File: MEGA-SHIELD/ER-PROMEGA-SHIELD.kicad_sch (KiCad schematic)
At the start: 1 part

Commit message: feat: cambios
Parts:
- added J10, J4, J6, J7, J9: Screw_Terminal_01x10, symbol Connector:Screw_Terminal_01x10
- added J11: Screw_Terminal_01x07, symbol Connector:Screw_Terminal_01x07
- added J5: Screw_Terminal_01x06, symbol Connector:Screw_Terminal_01x06
- added J8: Screw_Terminal_01x04, symbol Connector:Screw_Terminal_01x04
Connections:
- net at A1.A0: now also J10.1 (Pin_1)
- net at A1.A1: now also J10.2 (Pin_2)
- net at A1.A10: now also J11.1 (Pin_1)
- net at A1.A11: now also J11.2 (Pin_2)
- net at A1.A12: now also J11.3 (Pin_3)
- net at A1.A13: now also J11.4 (Pin_4)
- net at A1.A14: now also J11.5 (Pin_5)
- net at A1.A15: now also J11.6 (Pin_6)
- net at A1.A2: now also J10.3 (Pin_3)
- net at A1.A3: now also J10.4 (Pin_4)
- net at A1.A4: now also J10.5 (Pin_5)
- net at A1.A5: now also J10.6 (Pin_6)
- net at A1.A6: now also J10.7 (Pin_7)
- net at A1.A7: now also J10.8 (Pin_8)
- net at A1.A8: now also J10.9 (Pin_9)
- net at A1.A9: now also J10.10 (Pin_10)
- net at A1.AREF: now also J11.7 (Pin_7)
- net at A1.D0 (D0/RX0): now also J9.1 (Pin_1)
- net at A1.D1 (D1/TX0): now also J9.2 (Pin_2)
- net at A1.D10: now also J4.9 (Pin_9)
- net at A1.D11: now also J4.10 (Pin_10)
- net at A1.D12: now also J5.1 (Pin_1)
- net at A1.D13: now also J5.2 (Pin_2)
- net at A1.D14 (D14/TX3): now also J9.8 (Pin_8)
- net at A1.D15 (D15/RX3): now also J9.7 (Pin_7)
- net at A1.D16 (D16/TX2): now also J9.6 (Pin_6)
- net at A1.D17 (D17/RX2): now also J9.5 (Pin_5)
- net at A1.D18 (D18/TX1): now also J9.4 (Pin_4)
- net at A1.D19 (D19/RX1): now also J9.3 (Pin_3)
- net at A1.D2 (D2_INT0): now also J4.1 (Pin_1)
- net at A1.D20 (D20/SDA): now also J9.9 (Pin_9)
- net at A1.D21 (D21/SCL): now also J9.10 (Pin_10)
- net at A1.D22: now also J5.3 (Pin_3)
- net at A1.D23: now also J5.4 (Pin_4)
- net at A1.D24: now also J5.5 (Pin_5)
- net at A1.D25: now also J5.6 (Pin_6)
- net at A1.D3 (D3_INT1): now also J4.2 (Pin_2)
- net at A1.D30: now also J6.1 (Pin_1)
- net at A1.D31: now also J6.2 (Pin_2)
- net at A1.D32: now also J6.3 (Pin_3)
- net at A1.D33: now also J6.4 (Pin_4)
- net at A1.D34: now also J6.5 (Pin_5)
- net at A1.D35: now also J6.6 (Pin_6)
- net at A1.D36: now also J6.7 (Pin_7)
- net at A1.D37: now also J6.8 (Pin_8)
- net at A1.D38: now also J6.9 (Pin_9)
- net at A1.D39: now also J6.10 (Pin_10)
- net at A1.D4: now also J4.3 (Pin_3)
- net at A1.D40: now also J7.1 (Pin_1)
- net at A1.D41: now also J7.2 (Pin_2)
- net at A1.D42: now also J7.3 (Pin_3)
- net at A1.D43: now also J7.4 (Pin_4)
- net at A1.D44: now also J7.5 (Pin_5)
- net at A1.D45: now also J7.6 (Pin_6)
- net at A1.D46: now also J7.7 (Pin_7)
- net at A1.D47: now also J7.8 (Pin_8)
- net at A1.D48: now also J7.9 (Pin_9)
- net at A1.D49: now also J7.10 (Pin_10)
- net at A1.D5: now also J4.4 (Pin_4)
- net at A1.D50 (D50_MISO): now also J8.1 (Pin_1)
- net at A1.D51 (D51_MOSI): now also J8.2 (Pin_2)
- net at A1.D52 (D52_SCK): now also J8.3 (Pin_3)
- net at A1.D53 (D53_CS): now also J8.4 (Pin_4)
- net at A1.D6: now also J4.5 (Pin_5)
- net at A1.D7: now also J4.6 (Pin_6)
- net at A1.D8: now also J4.7 (Pin_7)
- net at A1.D9: now also J4.8 (Pin_8)

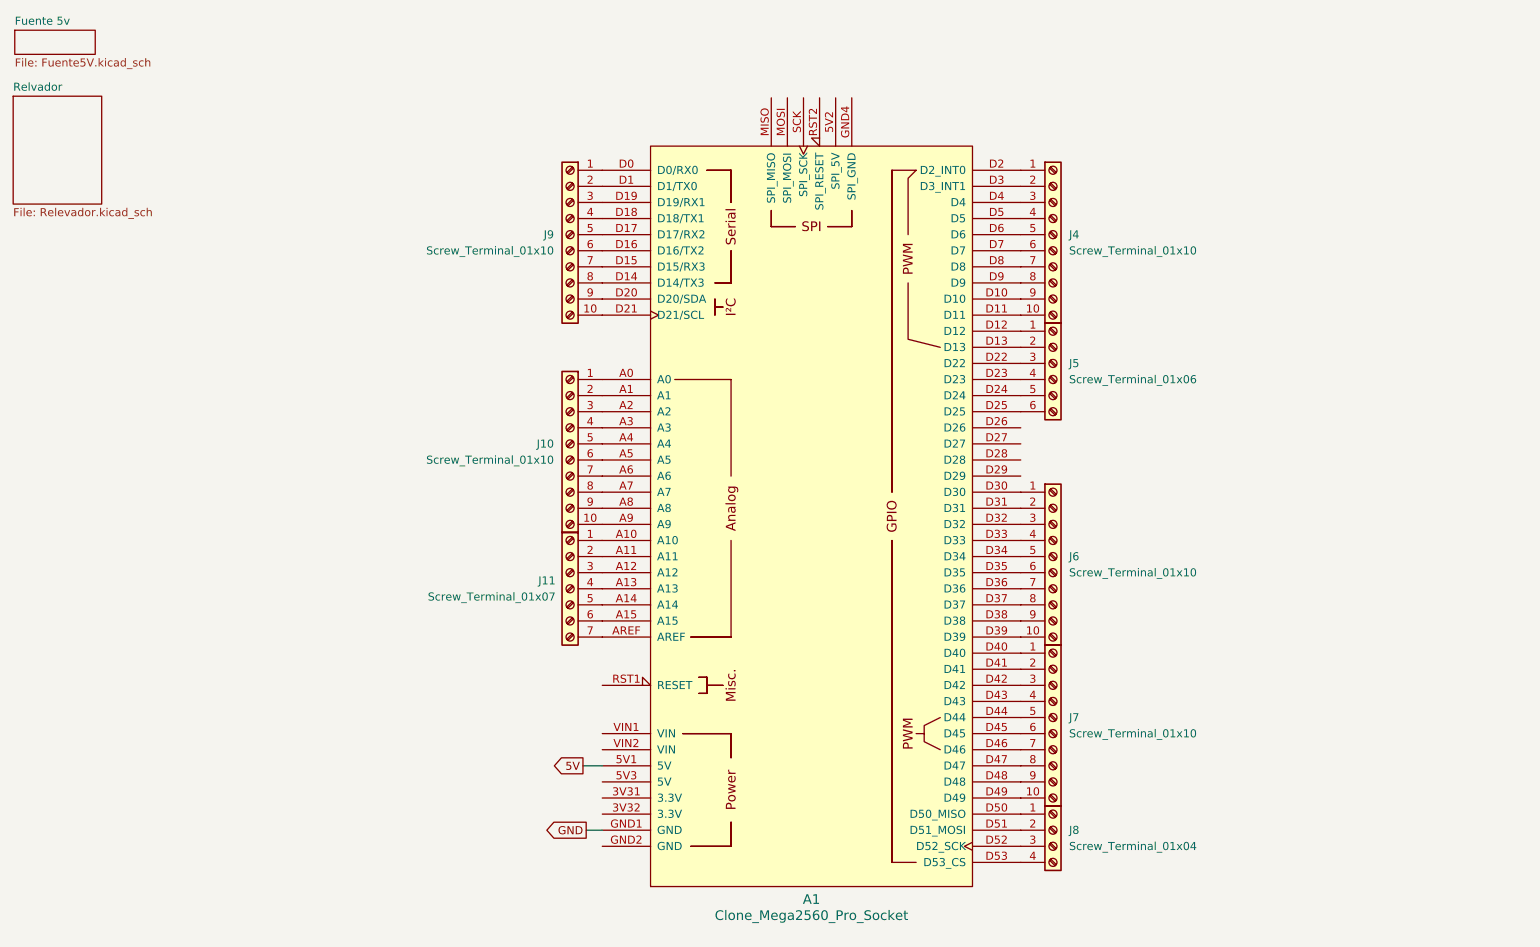
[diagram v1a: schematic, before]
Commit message: feat: agrege reles y optos
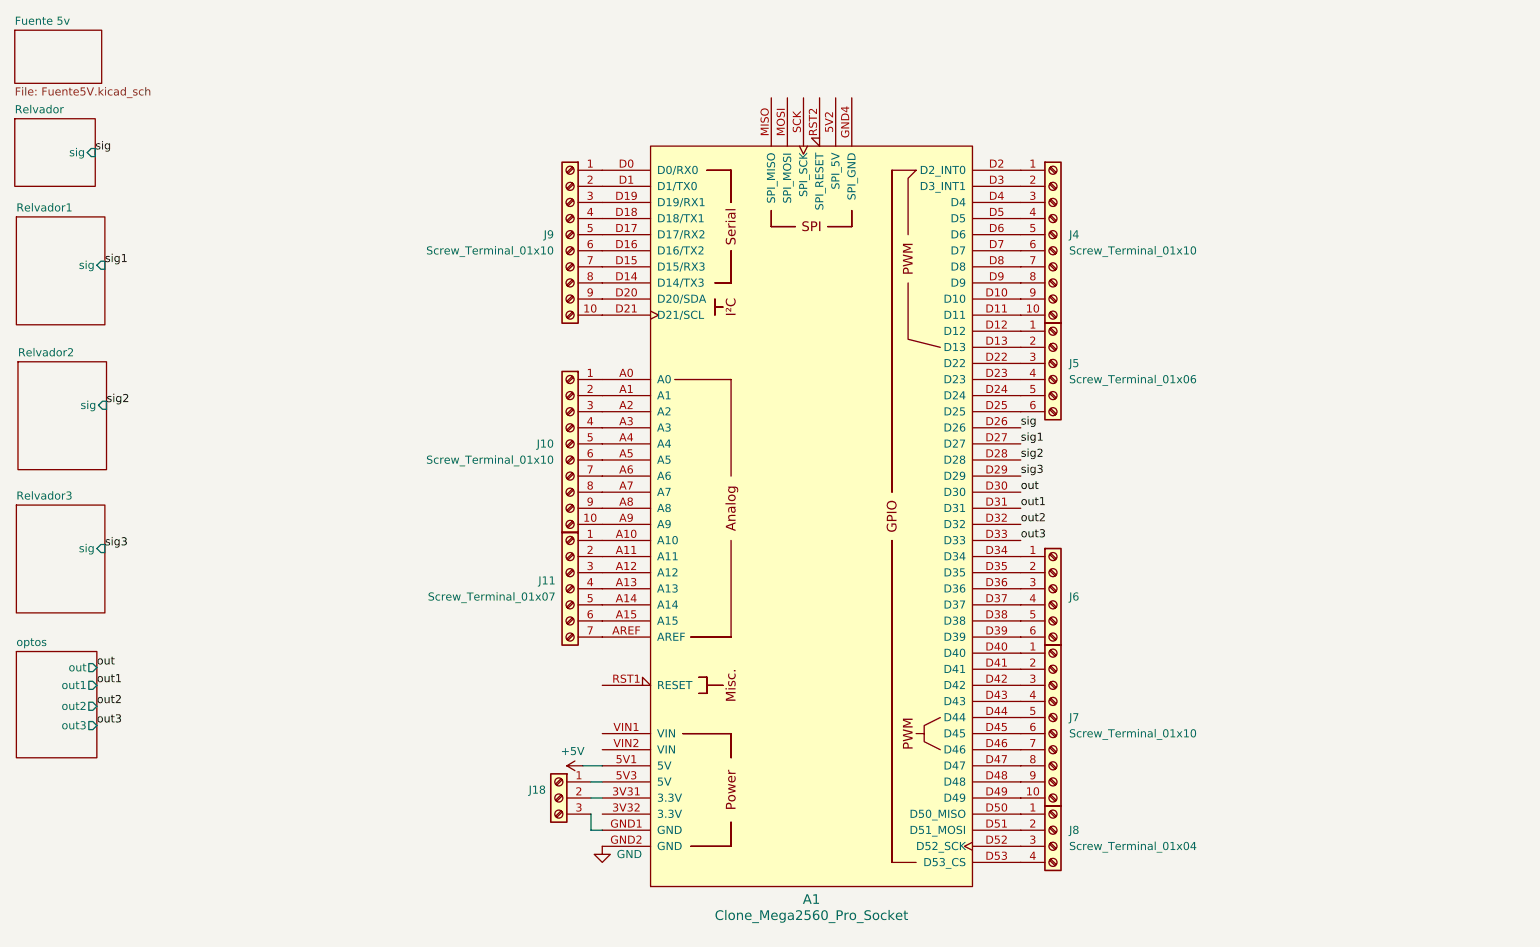
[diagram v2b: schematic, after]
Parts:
- removed J6: Screw_Terminal_01x10, symbol Connector:Screw_Terminal_01x10
- added J18: 1x3, TerminalBlock_Phoenix:TerminalBlock_Phoenix_MPT-0,5-3-2.54_1x03_P2.54mm_Horizontal, symbol Connector:Screw_Terminal_01x03
- added J6: Screw_Terminal_01x06, TerminalBlock_Phoenix:TerminalBlock_Phoenix_MPT-0,5-6-2.54_1x06_P2.54mm_Horizontal, symbol Connector:Screw_Terminal_01x06
- J10, J4, J7, J9: footprint (none) -> TerminalBlock_Phoenix:TerminalBlock_Phoenix_MPT-0,5-10-2.54_1x10_P2.54mm_Horizontal
- J11: footprint (none) -> TerminalBlock_Phoenix:TerminalBlock_Phoenix_MPT-0,5-7-2.54_1x07_P2.54mm_Horizontal
- J5: footprint (none) -> TerminalBlock_Phoenix:TerminalBlock_Phoenix_MPT-0,5-6-2.54_1x06_P2.54mm_Horizontal
- J8: footprint (none) -> TerminalBlock_Phoenix:TerminalBlock_Phoenix_MPT-0,5-4-2.54_1x04_P2.54mm_Horizontal
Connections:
- net GND: now also A1.GND2 (GND); no longer A1.GND1 (GND)
- net at A1.3V31 (3.3V): now also J18.2 (Pin_2)
- net at A1.5V3 (5V): now also J18.1 (Pin_1)
- net sig: now reaches A1.D26
- net sig1: now reaches A1.D27
- net sig2: now reaches A1.D28
- net sig3: now reaches A1.D29
- net out: now reaches A1.D30
- net out1: now reaches A1.D31
- net out2: now reaches A1.D32
- net out3: now reaches A1.D33
- net at A1.D34: now also J6.1 (Pin_1)
- net at A1.D35: now also J6.2 (Pin_2)
- net at A1.D36: now also J6.3 (Pin_3)
- net at A1.D37: now also J6.4 (Pin_4)
- net at A1.D38: now also J6.5 (Pin_5)
- net at A1.D39: now also J6.6 (Pin_6)
- net 5V renamed +5V
- new net: A1.GND1 (GND), J18.3 (Pin_3)
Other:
- added sheet Relvador1 (Relevador.kicad_sch)
- added sheet Relvador2 (Relevador.kicad_sch)
- added sheet Relvador3 (Relevador.kicad_sch)
- added sheet optos (optos.kicad_sch)
- sheet Relvador ports: added sig; removed none

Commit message: feat: avances2
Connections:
- net +5V: now also J18.1 (Pin_1)
- net at A1.5V3 (5V): no longer J18.1 (Pin_1)
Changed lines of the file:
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@@
 (kicad_sch (version 20230121) (generator eeschema)
   (paper "A4")
+  (junction (at 107.442 133.096) (diameter 0) (color 0 0 0 0)
+  )
   (wire (pts (xy 107.442 140.716) (xy 107.442 143.256))
     (stroke (width 0) (type default))
@@
     (stroke (width 0) (type default))
   )
-  (wire (pts (xy 106.172 133.096) (xy 109.22 133.096))
+  (wire (pts (xy 106.172 133.096) (xy 107.442 133.096))
     (stroke (width 0) (type default))
   )
-  (wire (pts (xy 109.22 135.636) (xy 107.442 135.636))
+  (wire (pts (xy 107.442 135.636) (xy 107.442 133.096))
     (stroke (width 0) (type default))
   )
+  (wire (pts (xy 107.442 133.096) (xy 109.22 133.096))
+    (stroke (width 0) (type default))
+  )

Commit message: feat: terminando ruteado.
termine ruteado y empezaria con la serigrafia
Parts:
- J9: footprint TerminalBlock_Phoenix:TerminalBlock_Phoenix_MPT-0,5-10-2.54_1x10_P2.54mm_Horizontal -> TerminalBlock_Phoenix:TerminalBlock_Phoenix_MPT-0,5-8-2.54_1x08_P2.54mm_Horizontal; symbol Connector:Screw_Terminal_01x10 -> Connector:Screw_Terminal_01x08
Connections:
- net GND: now also A1.GND1 (GND), J18.3 (Pin_3)
- net at J9.1 (Pin_1): now also A1.D19 (D19/RX1); no longer A1.D0 (D0/RX0)
- net at A1.D21 (D21/SCL): now also J9.8 (Pin_8); no longer J9.10 (Pin_10)
- net at J9.2 (Pin_2): now also A1.D18 (D18/TX1); no longer A1.D1 (D1/TX0)
- net at J9.3 (Pin_3): now also A1.D17 (D17/RX2); no longer A1.D19 (D19/RX1)
- net at J9.4 (Pin_4): now also A1.D16 (D16/TX2); no longer A1.D18 (D18/TX1)
- net at J9.5 (Pin_5): now also A1.D15 (D15/RX3); no longer A1.D17 (D17/RX2)
- net at J9.6 (Pin_6): now also A1.D14 (D14/TX3); no longer A1.D16 (D16/TX2)
- net at J9.7 (Pin_7): now also A1.D20 (D20/SDA); no longer A1.D15 (D15/RX3)
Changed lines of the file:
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@@
   (junction (at 107.442 133.096) (diameter 0) (color 0 0 0 0)
+  )
+  (junction (at 109.22 145.796) (diameter 0) (color 0 0 0 0)
+  )
+  (junction (at 109.22 143.256) (diameter 0) (color 0 0 0 0)
+  )
+  (wire (pts (xy 109.22 143.256) (xy 109.22 145.796))
+    (stroke (width 0) (type default))
   )
   (wire (pts (xy 107.442 140.716) (xy 107.442 143.256))
@@
     (effects (font (size 1.27 1.27)) (justify left bottom))
   )
-  (symbol (lib_id "Connector:Screw_Terminal_01x10") (at 104.14 49.276 0) (mirror y) (unit 1)
+  (symbol (lib_id "Connector:Screw_Terminal_01x08") (at 104.14 51.816 0) (mirror y) (unit 1)
     (in_bom yes) (on_board yes) (dnp no)
-    (property "Reference" "J9" (at 101.6 49.276 0)
+    (property "Reference" "J9" (at 101.6 51.816 0)
       (effects (font (size 1.27 1.27)) (justify left))
     )
-    (property "Value" "Screw_Terminal_01x10" (at 101.6 51.816 0)
+    (property "Value" "Screw_Terminal_01x10" (at 101.6 54.356 0)
       (effects (font (size 1.27 1.27)) (justify left))
     )
-    (property "Footprint" "TerminalBlock_Phoenix:TerminalBlock_Phoenix_MPT-0,5-10-2.54_1x10_P2.54mm_Horizontal" (at 104.14 49.276 0)
+    (property "Footprint" "TerminalBlock_Phoenix:TerminalBlock_Phoenix_MPT-0,5-8-2.54_1x08_P2.54mm_Horizontal" (at 104.14 51.816 0)
       (effects (font (size 1.27 1.27)) hide)
     )
-    (property "Datasheet" "~" (at 104.14 49.276 0)
+    (property "Datasheet" "~" (at 104.14 51.816 0)
       (effects (font (size 1.27 1.27)) hide)
     )
     (pin "1")
-    (pin "10")
     (pin "2")
     (pin "3")
@@
     (pin "7")
     (pin "8")
-    (pin "9")
     (instances
       (project "ER-PROMEGA-SHIELD"

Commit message: develop: version 1.1
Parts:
- J1: renamed from J18; footprint TerminalBlock_Phoenix:TerminalBlock_Phoenix_MPT-0,5-3-2.54_1x03_P2.54mm_Horizontal -> Connector_Phoenix_MC:PhoenixContact_MCV_1,5_3-G-3.81_1x03_P3.81mm_Vertical
- J2: renamed from J9; footprint TerminalBlock_Phoenix:TerminalBlock_Phoenix_MPT-0,5-8-2.54_1x08_P2.54mm_Horizontal -> Connector_Phoenix_MC:PhoenixContact_MCV_1,5_8-G-3.81_1x08_P3.81mm_Vertical
- J3: renamed from J10; footprint TerminalBlock_Phoenix:TerminalBlock_Phoenix_MPT-0,5-10-2.54_1x10_P2.54mm_Horizontal -> Connector_Phoenix_MC:PhoenixContact_MCV_1,5_10-G-3.81_1x10_P3.81mm_Vertical
- J4: renamed from J11; footprint TerminalBlock_Phoenix:TerminalBlock_Phoenix_MPT-0,5-7-2.54_1x07_P2.54mm_Horizontal -> Connector_Phoenix_MC:PhoenixContact_MCV_1,5_7-G-3.81_1x07_P3.81mm_Vertical
- J5: renamed from J4; footprint TerminalBlock_Phoenix:TerminalBlock_Phoenix_MPT-0,5-10-2.54_1x10_P2.54mm_Horizontal -> Connector_Phoenix_MC:PhoenixContact_MCV_1,5_10-G-3.81_1x10_P3.81mm_Vertical
- J6: renamed from J5; footprint TerminalBlock_Phoenix:TerminalBlock_Phoenix_MPT-0,5-6-2.54_1x06_P2.54mm_Horizontal -> Connector_Phoenix_MC:PhoenixContact_MCV_1,5_6-G-3.81_1x06_P3.81mm_Vertical
- J7: renamed from J6; footprint TerminalBlock_Phoenix:TerminalBlock_Phoenix_MPT-0,5-6-2.54_1x06_P2.54mm_Horizontal -> Connector_Phoenix_MC:PhoenixContact_MCV_1,5_6-G-3.81_1x06_P3.81mm_Vertical
- J8: renamed from J7; footprint TerminalBlock_Phoenix:TerminalBlock_Phoenix_MPT-0,5-10-2.54_1x10_P2.54mm_Horizontal -> Connector_Phoenix_MC:PhoenixContact_MCV_1,5_10-G-3.81_1x10_P3.81mm_Vertical
- J9: renamed from J8; footprint TerminalBlock_Phoenix:TerminalBlock_Phoenix_MPT-0,5-4-2.54_1x04_P2.54mm_Horizontal -> Connector_Phoenix_MC:PhoenixContact_MCV_1,5_4-G-3.81_1x04_P3.81mm_Vertical
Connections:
- net sig is gone; now on net sig1: A1.D26
- net +5V: now also J1.3 (Pin_3); no longer J1.1 (Pin_1)
- net GND: now also J1.1 (Pin_1); no longer J1.3 (Pin_3)
- net sig1: no longer A1.D27
- net sig2: now also A1.D27; no longer A1.D28
- net sig3: now also A1.D28; no longer A1.D29
- net at J2.1 (Pin_1): now also A1.D21 (D21/SCL); no longer A1.D19 (D19/RX1)
- net at J2.2 (Pin_2): now also A1.D20 (D20/SDA); no longer A1.D18 (D18/TX1)
- net at J2.3 (Pin_3): now also A1.D14 (D14/TX3); no longer A1.D17 (D17/RX2)
- net at J2.4 (Pin_4): now also A1.D15 (D15/RX3); no longer A1.D16 (D16/TX2)
- net at J2.5 (Pin_5): now also A1.D16 (D16/TX2); no longer A1.D15 (D15/RX3)
- net at J2.6 (Pin_6): now also A1.D17 (D17/RX2); no longer A1.D14 (D14/TX3)
- net at J2.7 (Pin_7): now also A1.D18 (D18/TX1); no longer A1.D20 (D20/SDA)
- net at J2.8 (Pin_8): now also A1.D19 (D19/RX1); no longer A1.D21 (D21/SCL)
- net at J8.1 (Pin_1): now also A1.D49; no longer A1.D40
- net at J8.10 (Pin_10): now also A1.D40; no longer A1.D49
- net at J8.2 (Pin_2): now also A1.D48; no longer A1.D41
- net at J8.3 (Pin_3): now also A1.D47; no longer A1.D42
- net at J8.4 (Pin_4): now also A1.D46; no longer A1.D43
- net at J8.5 (Pin_5): now also A1.D45; no longer A1.D44
- net at J8.6 (Pin_6): now also A1.D44; no longer A1.D45
- net at J8.7 (Pin_7): now also A1.D43; no longer A1.D46
- net at J8.8 (Pin_8): now also A1.D42; no longer A1.D47
- net at J8.9 (Pin_9): now also A1.D41; no longer A1.D48
- net at J7.1 (Pin_1): now also A1.D39; no longer A1.D34
- net at J7.2 (Pin_2): now also A1.D38; no longer A1.D35
- net at J7.3 (Pin_3): now also A1.D37; no longer A1.D36
- net at J7.4 (Pin_4): now also A1.D36; no longer A1.D37
- net at J7.5 (Pin_5): now also A1.D35; no longer A1.D38
- net at J7.6 (Pin_6): now also A1.D34; no longer A1.D39
- net at A1.3V31 (3.3V): no longer J1.2 (Pin_2)
- net at A1.3V32 (3.3V): now also J1.2 (Pin_2)
- new net sig4: A1.D29
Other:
- removed sheet Relvador
- removed sheet Relvador1
- removed sheet Relvador2
- removed sheet Relvador3
- added sheet uln2003 (uln2003.kicad_sch)
- moved on the sheet: A1, J1, J2, J3, J4, J5, J6, J7, J8, J9
